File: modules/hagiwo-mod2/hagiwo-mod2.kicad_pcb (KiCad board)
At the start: 2 copper layers, 136 x 72 mm, 72 parts, among them J1 JST-SH, J10 Conn_01x02_MountingPin, J2 JST-SH, J3 JST-SH, J4 Conn_01x02_MountingPin, J6 JST-SH, J7 Conn_01x02_MountingPin, J8 JST SH, 4P, VT, SMT, J9 Conn_01x02_MountingPin, U1 TL074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

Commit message: Add Rev.B notes and changes. Work in progress.
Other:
- board text added: "Re-evaluate zip-tie hole placement."
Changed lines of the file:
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@@
 	(title_block
 		(title "Hagiwo MOD2 Module")
-		(date "2025-09-08")
-		(rev "A")
+		(date "2025-09-30")
+		(rev "B")
 		(company "by Circuit Monkey")
 		(comment 1 "for ASMR - Advanced Synth Module Rack")
@@
 		)
 	)
+	(gr_text "Re-evaluate zip-tie hole placement."
+		(at 173.4 58.7 0)
+		(layer "Cmts.User")
+		(effects
+			(font
+				(size 1 1)
+				(thickness 0.1)
+			)
+			(justify left bottom)
+		)
+	)

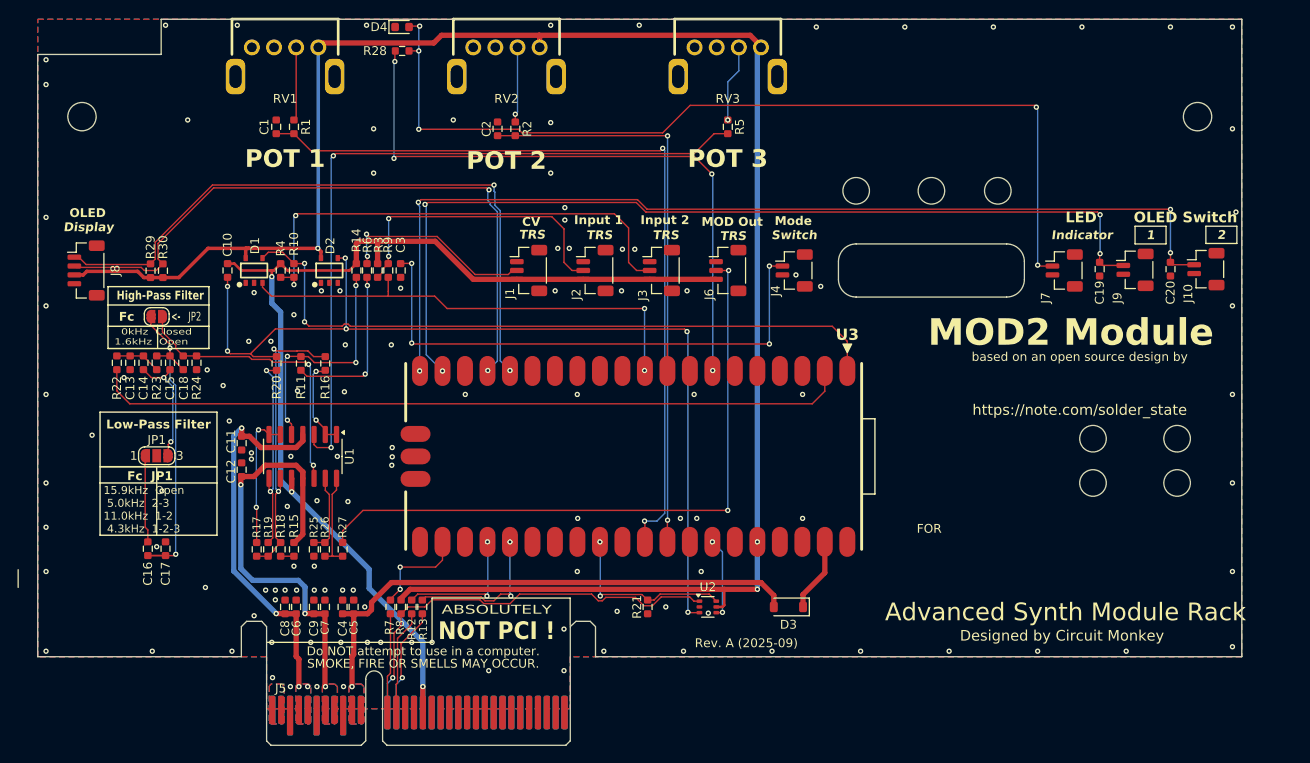
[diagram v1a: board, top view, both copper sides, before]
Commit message: Rev.B Tuning. Part values mostly.
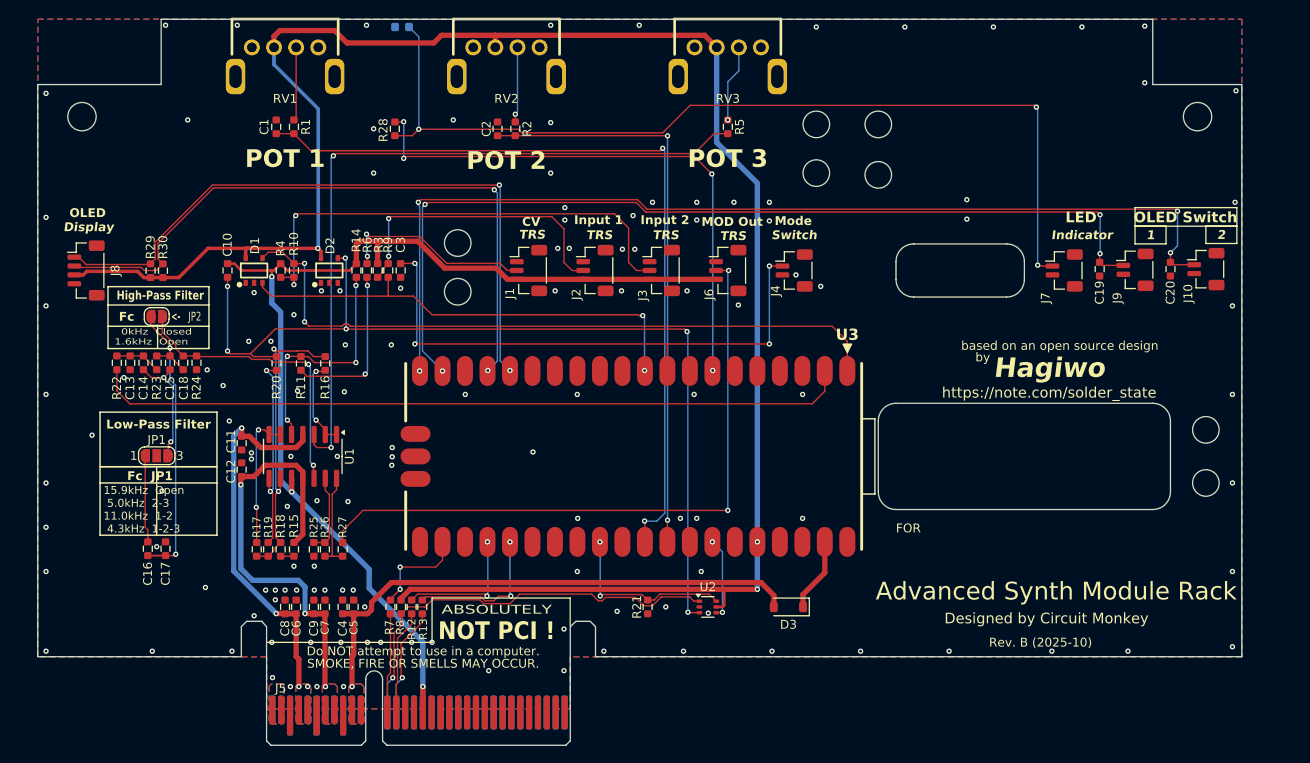
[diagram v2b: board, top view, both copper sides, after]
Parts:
- C11, C12, C5, C8, C9: value 1uF/50V -> 1uF/25V
- C18: value 0.01uF -> 1uF
- C6, C7: value 10uF/50V -> 10uF/25V
- D4: moved to B.Cu
- R15: value 33.0K -> 45.0K
- R24: value 10K -> 100K
- R8: value 10K -> 33K
- moved R28 8.84 mm to (122.4, 55.0), turned to 90 degrees
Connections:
- RV1 pad 1: +3V3 -> GND_CH
- RV1 pad 3: GND_CH -> +3V3
- RV2 pad 1: +3V3 -> GND_CH
- RV2 pad 3: GND_CH -> +3V3
- RV3 pad 1: +3V3 -> GND_CH
- RV3 pad 3: GND_CH -> +3V3
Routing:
- net LED: track 71.3 -> 63.3 mm
- net +3V3: track 212.3 -> 218.0 mm
- net OLED_SW2: track 113.4 -> 114.5 mm
- net Net-(D4-A): track 104.9 -> 105.9 mm, vias 5 -> 3
- net IN_1: track 53.8 -> 53.2 mm
- net GND_CH: track 0.12 -> 0.27 mm, vias 122 -> 132
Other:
- outline, holes or cut-outs redrawn
- board text added: "Rev. B (2025-10)"
- board text added: "based on an open source design"
- board text added: "by"
- board text removed: "Re-evaluate zip-tie hole placement."
- board text removed: "Rev. A (2025-09)"
- board text removed: "based on an open source design by"
